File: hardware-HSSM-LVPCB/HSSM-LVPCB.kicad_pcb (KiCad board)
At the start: 4 copper layers, 36 x 12 mm, 57 parts, among them J1 UFL_R_SMT_1_10, J2 LPPB061NGCN-RC, Q1 Q_MOSFET_N_BSS123, Q2 Q_MOSFET_N_BSS123, U1 ESP32-C6, U2 W25Q64JVSSIQ_SOIC-8, X1 X_40MHz_SMD_ECS-2520SMV-400-F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

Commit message: [#13] PCB routing WIP GPIO
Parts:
- moved S2 0.23 mm to (150.6, 114.6)
- moved S3 0.20 mm to (142.1, 114.6)
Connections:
- U1 pad 16: unconnected-(U1-GPIO10-Pad16) -> /GPIO_Q2
- U1 pad 17: /GPIO_S2 -> /GPIO_S3
- U1 pad 18: unconnected-(U1-GPIO12-Pad18) -> /GPIO_S2
- U1 pad 6: /GPIO_Q2 -> unconnected-(U1-XTAL_32K_P-Pad6)
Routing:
- net /Enable: track 0.99 -> 24.3 mm, vias 1 -> 3
- net /BOOT: track 2.46 -> 17.0 mm, vias 1 -> 2
- net /S2_sym: track 13.4 -> 10.7 mm
- net /GPIO_Q2: track 40.6 -> 42.8 mm
- net /GPIO_S3: track 28.8 -> 30.7 mm, vias 2 -> 3
- net unconnected-(U1-GPIO10-Pad16): track 1.68 -> 0.00 mm, vias 1 -> 0
- net unconnected-(U1-GPIO12-Pad18): track 1.10 -> 0.00 mm, vias 1 -> 0
- net unconnected-(U1-XTAL_32K_P-Pad6): track 0.00 -> 1.01 mm, vias 0 -> 1
- net /GPIO_S2: track 29.5 -> 30.2 mm

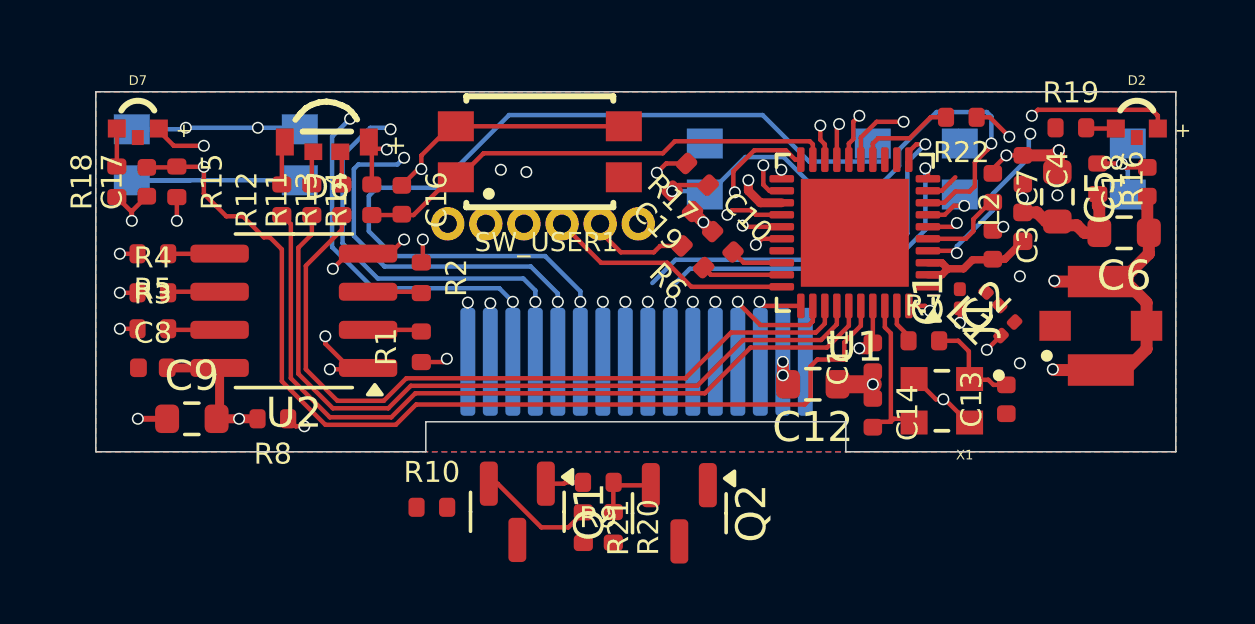
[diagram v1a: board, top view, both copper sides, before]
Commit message: Add additional signals to FCB between PCBs
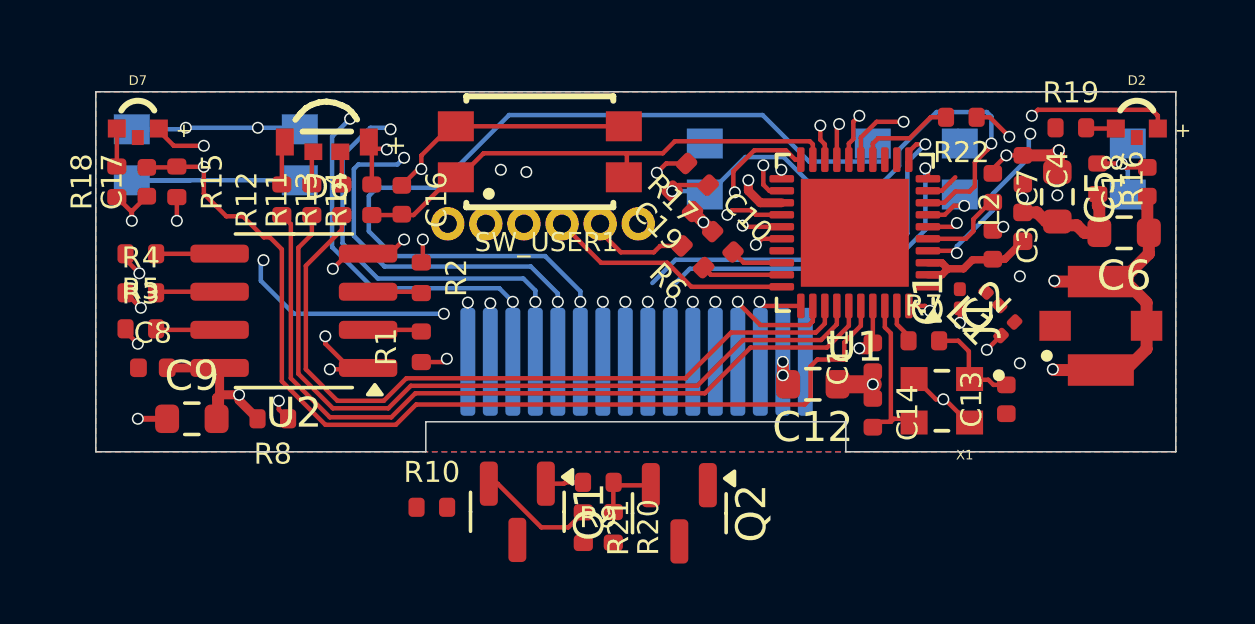
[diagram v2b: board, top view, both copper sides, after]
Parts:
- moved R3 0.40 mm to (120.5, 119.9)
- moved R4 0.40 mm to (120.5, 118.7)
- moved R5 0.40 mm to (120.5, 117.4)
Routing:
- net /GPIO_Q1: track 24.6 -> 28.2 mm, vias 2 -> 4
- net /S_set: track 16.3 -> 17.1 mm
- net Net-(U1-SPICLK): track 26.7 -> 26.0 mm
- net Net-(U1-SPID): track 24.2 -> 23.6 mm

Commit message: [#13] PCB routing WIP prog signals
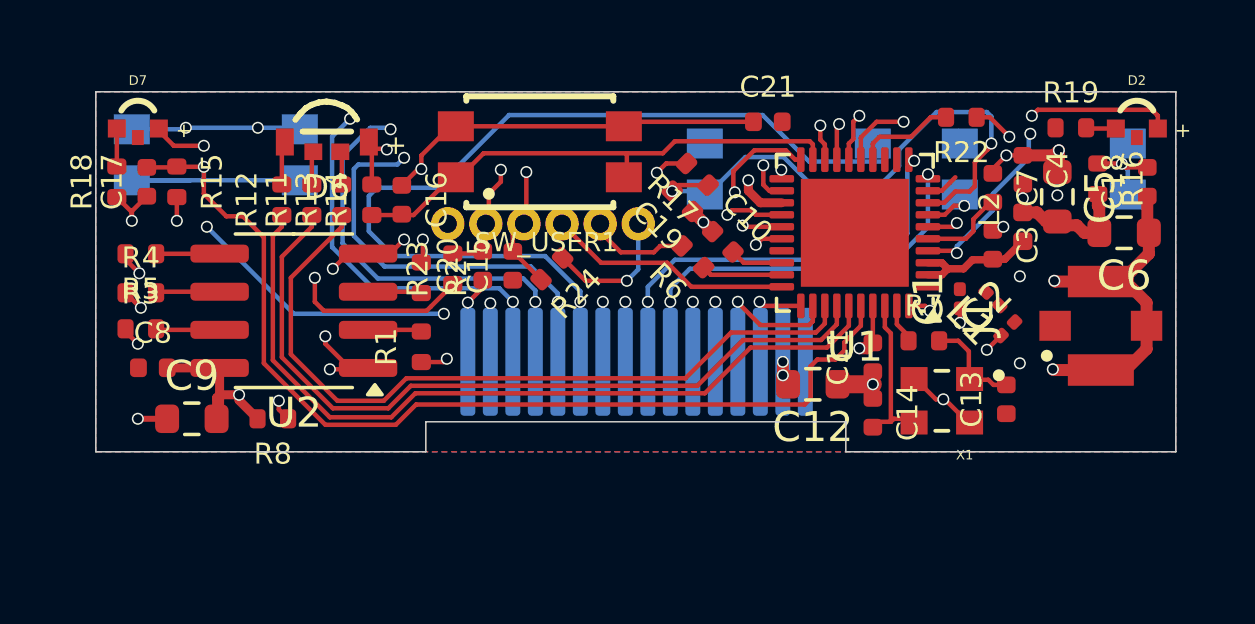
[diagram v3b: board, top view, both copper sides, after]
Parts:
- removed Q1, Q2: Q_MOSFET_N_BSS123, HSSM-LVPCB:SOT-23
- removed R10, R9: R_499R_1pct_0402_RC0402FR-07499RL, HSSM-LVPCB:R_0402
- removed R20, R21: R_10k_1pct_0402_RC0402FR-0710KL, HSSM-LVPCB:R_0402
- added C15: C_0u1_10pct_50V_0402_GRM155R71H104KE14D, HSSM-LVPCB:C_0402, F.Cu at (132.9, 117.8)
- added C20: C_0u1_10pct_50V_0402_GRM155R71H104KE14D, HSSM-LVPCB:C_0402, F.Cu at (131.9, 117.8)
- added C21: C_0u1_10pct_50V_0402_GRM155R71H104KE14D, HSSM-LVPCB:C_0402, F.Cu at (141.4, 113.0)
- added R23: R_10k_1pct_0402_RC0402FR-0710KL, HSSM-LVPCB:R_0402, F.Cu at (130.9, 117.9)
- added R24: R_10k_1pct_0402_RC0402FR-0710KL, HSSM-LVPCB:R_0402, F.Cu at (134.2, 117.9)
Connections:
- CON1 pad 10: unconnected-(CON1-Pad10) -> /P_MEAS_RST
- CON1 pad 5: unconnected-(CON1-Pad5) -> /DO3
- CON1 pad 6: unconnected-(CON1-Pad6) -> /DO2
- CON1 pad 7: /DEV_TX -> /LP_UART_RXD
- CON1 pad 8: /DEV_RX -> /LP_UART_TXD
- J2 pad 2: /DTR -> /BOOT
- J2 pad 3: /RTS -> /Enable
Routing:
- net +3V3: track 13.5 -> 23.9 mm, vias 9 -> 11
- net GND: track 46.5 -> 51.8 mm
- net /Enable: track 24.3 -> 28.5 mm
- net /BOOT: track 17.0 -> 21.0 mm
- net /RTS: track 3.96 -> 0.00 mm
- net /DTR: track 2.28 -> 0.00 mm
- net /LP_UART_RXD: track 11.5 -> 13.8 mm, vias 1 -> 2
- net unconnected-(CON1-Pad6): track 2.03 -> 0.00 mm, vias 1 -> 0
- net /DO2: track 0.00 -> 2.03 mm, vias 0 -> 1
- net unconnected-(CON1-Pad10): track 2.00 -> 0.00 mm, vias 1 -> 0
- net /P_MEAS_RST: track 0.00 -> 2.00 mm, vias 0 -> 1
- net /DEV_TX: track 2.00 -> 0.00 mm, vias 1 -> 0
- net /DEV_RX: track 2.00 -> 0.00 mm, vias 1 -> 0
- net unconnected-(CON1-Pad5): track 1.97 -> 0.00 mm, vias 1 -> 0
- net /DO3: track 0.00 -> 1.97 mm, vias 0 -> 1
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
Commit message: [#13] PCB routing WIP GPIO
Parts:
- moved C21 6.15 mm to (147.6, 112.8)
- moved R22 1.43 mm to (147.8, 114.3), turned to 90 degrees
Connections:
- U1 pad 12: unconnected-(U1-MTCK-Pad12) -> /S3_sym
- U1 pad 8: /S3_sym -> unconnected-(U1-GPIO2-Pad8)
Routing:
- net /P_MEAS_RST: track 2.00 -> 25.6 mm
- net /DO2: track 2.03 -> 12.9 mm, vias 1 -> 0
- net /DO3: track 1.97 -> 11.3 mm, vias 1 -> 0
- net /Enable: track 28.5 -> 21.8 mm, vias 3 -> 2
- net /S3_sym: track 18.9 -> 13.2 mm
- net unconnected-(U1-GPIO2-Pad8): track 0.00 -> 3.44 mm, vias 0 -> 1
- net /BOOT: track 21.0 -> 19.0 mm
- net unconnected-(U1-MTDO-Pad13): track 0.00 -> 1.53 mm, vias 0 -> 1
- net +3V3: track 23.9 -> 25.4 mm
- net unconnected-(U1-GPIO3-Pad9): track 1.10 -> 2.17 mm, vias 0 -> 1
- net /GPIO8: track 3.34 -> 2.45 mm, vias 0 -> 1
- net /GPIO_Q2: track 42.8 -> 43.7 mm
- net /GPIO_S3: track 30.7 -> 30.0 mm
- net /LP_UART_RXD: vias 2 -> 1
- net /LP_UART_TXD: vias 2 -> 1

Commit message: [#13] PCB routing WIP GPIO
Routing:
- net /DO3: track 11.3 -> 16.8 mm
- net /DO1: track 30.6 -> 28.0 mm
- net /DO2: track 12.9 -> 11.9 mm
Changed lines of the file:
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@@
+	)
+	(segment
+		(start 143.6 112.7)
+		(end 144.325 113.425)
+		(width 0.15)
+		(layer "In1.Cu")
+		(net 12)
+	)
+	(segment
+		(start 150.175 112.775)
+		(end 150.2 112.8)
+		(width 0.15)
+		(layer "In1.Cu")
+		(net 12)
+	)
+	(segment
+		(start 147.05 112.775)
+		(end 150.175 112.775)
+		(width 0.15)
+		(layer "In1.Cu")
+		(net 12)
+	)
+	(segment
+		(start 144.325 113.425)
+		(end 146.4 113.425)
+		(width 0.15)
+		(layer "In1.Cu")
+		(net 12)
+	)
+	(segment
+		(start 146.4 113.425)
+		(end 147.05 112.775)
+		(width 0.15)
+		(layer "In1.Cu")
+		(net 12)
 	)
 	(segment
@@
 		(start 127.475 112.9)
 		(end 126.875 113.5)
-		(width 0.15)
-		(layer "B.Cu")
-		(net 12)
-	)
-	(segment
-		(start 143.6 112.7)
-		(end 144.65 111.65)
-		(width 0.15)
-		(layer "B.Cu")
-		(net 12)
-	)
-	(segment
-		(start 144.65 111.65)
-		(end 149.05 111.65)
-		(width 0.15)
-		(layer "B.Cu")
-		(net 12)
-	)
-	(segment
-		(start 149.05 111.65)
-		(end 150.2 112.8)
 		(width 0.15)
 		(layer "B.Cu")
@@
 	)
 	(segment
-		(start 142.775 114.325)
-		(end 145.325 114.325)
-		(width 0.15)
-		(layer "B.Cu")
-		(net 41)
-	)
-	(segment
 		(start 130.35 115.2)
 		(end 132.975 112.575)
@@
 	)
 	(segment
-		(start 139.9 118.475)
-		(end 146.3 118.475)
+		(start 148.375 116.575)
+		(end 148.825 116.125)
+		(width 0.15)
+		(layer "B.Cu")
+		(net 42)
+	)
+	(segment
+		(start 147.45 118.475)
+		(end 148.375 117.55)
+		(width 0.15)
+		(layer "B.Cu")
+		(net 42)
+	)
+	(segment
+		(start 148.825 114.8)
+		(end 148.6 114.575)
+		(width 0.15)
+		(layer "B.Cu")
+		(net 42)
+	)
+	(segment
+		(start 147.234252 114.575)
+		(end 147.067126 114.407874)
+		(width 0.15)
+		(layer "B.Cu")
+		(net 42)
+	)
+	(segment
+		(start 148.375 117.55)
+		(end 148.375 116.575)
+		(width 0.15)
+		(layer "B.Cu")
+		(net 42)
+	)
+	(segment
+		(start 147.067126 114.407874)
+		(end 146.825 114.165748)
 		(width 0.15)
 		(layer "B.Cu")
@@
 	)
 	(segment
+		(start 148.825 116.125)
+		(end 148.825 114.8)
+		(width 0.15)
+		(layer "B.Cu")
+		(net 42)
+	)
+	(segment
+		(start 148.6 114.575)
+		(end 147.234252 114.575)
+		(width 0.15)
+		(layer "B.Cu")
+		(net 42)
+	)
+	(segment
+		(start 146.825 114.165748)
+		(end 146.825 114)
+		(width 0.15)
+		(layer "B.Cu")
+		(net 42)
+	)
+	(segment
+		(start 139.9 118.475)
+		(end 147.45 118.475)
+		(width 0.15)
+		(layer "B.Cu")
+		(net 42)
+	)
+	(segment
 		(start 139.65 119)
 		(end 139.65 118.725)
@@
 		(net 42)
 	)
-	(segment
-		(start 146.3 118.475)
-		(end 147.3 117.475)
-		(width 0.15)
-		(layer "B.Cu")
-		(net 42)
-	)
-	(segment
-		(start 147.3 117.475)
-		(end 147.3 116.55)
-		(width 0.15)
-		(layer "B.Cu")
-		(net 42)
-	)
 	(via
 		(at 135.9 119)
@@
 	)
 	(segment
+		(start 147.025 117.025)
+		(end 147.475 116.575)
+		(width 0.15)
+		(layer "B.Cu")
+		(net 45)
+	)
+	(segment
 		(start 138.9 118.45)
 		(end 139.125 118.225)
@@
 	)
 	(segment
-		(start 147.025 117.025)
-		(end 147.025 115.4)
-		(width 0.15)
-		(layer "B.Cu")
-		(net 45)
-	)
-	(segment
 		(start 147.65 115.325)
 		(end 148.125 115.325)
@@
 	)
 	(segment
-		(start 146.7375 114.75)
-		(end 146.7375 116.5125)
+		(start 146 115.4875)
+		(end 146 117.25)
 		(width 0.15)
 		(layer "B.Cu")
@@
 	)
 	(segment
-		(start 146.7375 116.5125)
+		(start 146.7375 114.75)
+		(end 146 115.4875)
+		(width 0.15)
+		(layer "B.Cu")
+		(net 51)
+	)
+	(segment
+		(start 138.15 118.55)
+		(end 138.15 121)
+		(width 0.15)
+		(layer "B.Cu")
+		(net 51)
+	)
+	(segment
+		(start 146 117.25)
 		(end 145.425 117.825)
 		(width 0.15)
@@
 	)
 	(segment
-		(start 138.15 118.55)
-		(end 138.15 121)
-		(width 0.15)
-		(layer "B.Cu")
-		(net 51)
-	)
-	(segment
 		(start 146.275 114.3)
 		(end 146.2375 114.2625)
@@
 	)
 	(segment
-		(start 146.05 114.525)
-		(end 146.05 116.725)
+		(start 137.4 121)
+		(end 137.4 118.5)
 		(width 0.15)
 		(layer "B.Cu")
@@
 	)
 	(segment
-		(start 146.05 116.725)
+		(start 145.725 117.05)
+		(end 145.725 115.05)
+		(width 0.15)
+		(layer "B.Cu")
+		(net 52)
+	)
+	(segment
+		(start 146.25 114.525)
+		(end 146.25 114.325)
+		(width 0.15)
+		(layer "B.Cu")
+		(net 52)
+	)
+	(segment
+		(start 138.325 117.575)
 		(end 145.2 117.575)
 		(width 0.15)
@@
 	)
 	(segment
+		(start 137.4 118.5)
+		(end 138.325 117.575)
+		(width 0.15)
+		(layer "B.Cu")
+		(net 52)
+	)
+	(segment
+		(start 145.725 115.05)
+		(end 146.25 114.525)
+		(width 0.15)
+		(layer "B.Cu")
+		(net 52)
+	)
+	(segment
+		(start 146.25 114.325)
+		(end 146.275 114.3)
+		(width 0.15)
+		(layer "B.Cu")
+		(net 52)
+	)
+	(segment
 		(start 145.2 117.575)
-		(end 138.325 117.575)
-		(width 0.15)
-		(layer "B.Cu")
-		(net 52)
-	)
-	(segment
-		(start 137.4 118.5)
-		(end 137.4 121)
-		(width 0.15)
-		(layer "B.Cu")
-		(net 52)
-	)
-	(segment
-		(start 138.325 117.575)
-		(end 137.4 118.5)
-		(width 0.15)
-		(layer "B.Cu")
-		(net 52)
-	)
-	(segment
-		(start 146.275 114.3)
-		(end 146.05 114.525)
-		(width 0.15)
-		(layer "B.Cu")
+		(end 145.725 117.05)
+		(width 0.15)
+		(layer "B.Cu")

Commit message: [#13] PCB routing WIP GPIO
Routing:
- net /S3_sym: track 13.2 -> 18.9 mm
- net /DO1: track 28.0 -> 32.7 mm
- net /P_MEAS_RST: track 25.6 -> 30.1 mm

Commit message: [#13] PCB routing
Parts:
- moved C10 1.36 mm to (138.6, 117.2)
- moved R6 1.12 mm to (137.8, 117.9)
- moved C19 0.12 mm to (138.4, 115.7)
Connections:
- U1 pad 13: unconnected-(U1-MTDO-Pad13) -> /DO1
- U1 pad 27: unconnected-(U1-GPIO15-Pad27) -> /P_MEAS_RST
- U1 pad 6: unconnected-(U1-XTAL_32K_P-Pad6) -> /DO2
- U1 pad 9: unconnected-(U1-GPIO3-Pad9) -> /DO3
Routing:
- net /P_MEAS_RST: track 30.1 -> 9.06 mm, vias 1 -> 2
- net GND: track 51.9 -> 59.4 mm, vias 22 -> 27
- net /GPIO8: track 2.45 -> 7.25 mm, vias 1 -> 2
- net unconnected-(U1-GPIO3-Pad9): track 2.17 -> 0.00 mm, vias 1 -> 0
- net /DO1: track 32.7 -> 34.8 mm, vias 1 -> 2
- net /DO3: track 16.8 -> 18.9 mm, vias 0 -> 1
- net unconnected-(U1-MTDO-Pad13): track 1.73 -> 0.00 mm, vias 1 -> 0
- net /S3_sym: track 18.9 -> 20.4 mm
- net Net-(U1-U0TXD): track 2.70 -> 3.98 mm
- net Net-(U1-VDDPST2): track 1.77 -> 3.05 mm
- net /U0TXD: track 3.36 -> 2.30 mm
- net unconnected-(U1-XTAL_32K_P-Pad6): track 1.01 -> 0.00 mm, vias 1 -> 0
- net Net-(U1-SPICLK): track 26.2 -> 25.3 mm
- net /DO2: track 11.9 -> 12.6 mm, vias 0 -> 1
- net Net-(U1-SPID): track 24.1 -> 24.7 mm

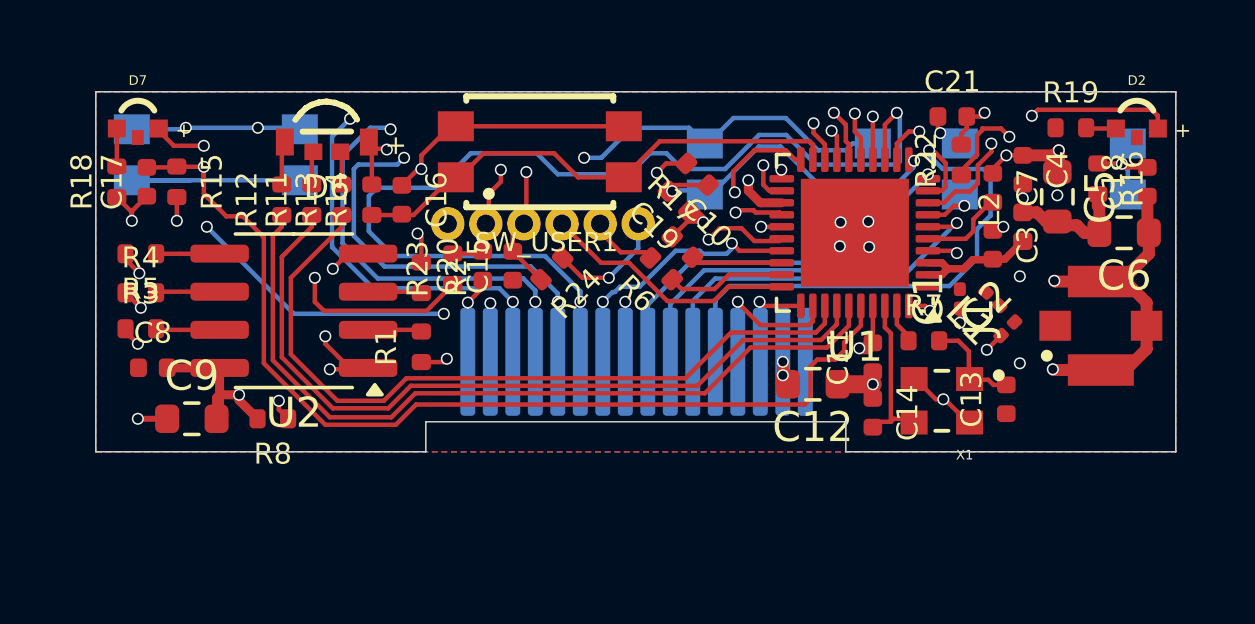
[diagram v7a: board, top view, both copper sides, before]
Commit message: [#12][#13] PCB change edge cuts
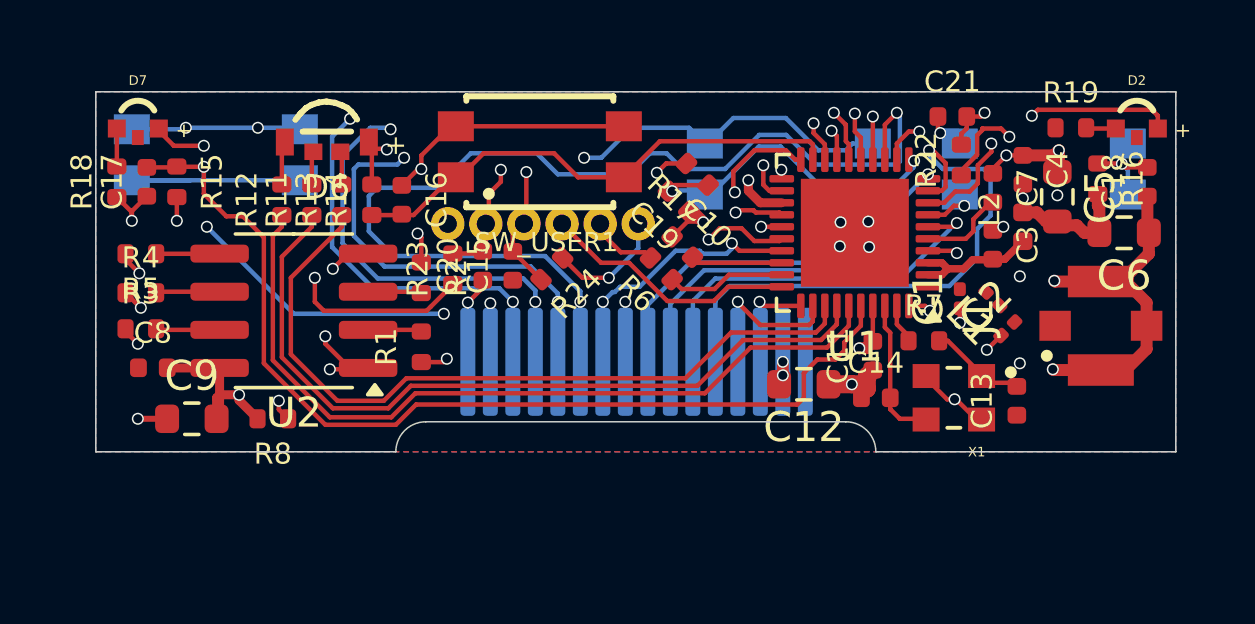
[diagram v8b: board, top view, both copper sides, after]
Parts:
- moved C14 0.51 mm to (145.0, 122.2), turned to 0 degrees
- moved X1 0.41 mm to (147.6, 122.2)
- moved C13 0.35 mm to (149.7, 122.3)
- moved C12 0.30 mm to (142.6, 121.8)
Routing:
- net GND: track 59.4 -> 60.9 mm
- net Net-(U1-XTAL_N): track 5.49 -> 4.85 mm
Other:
- outline, holes or cut-outs redrawn
